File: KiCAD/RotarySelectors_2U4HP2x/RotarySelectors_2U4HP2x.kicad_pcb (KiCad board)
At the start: 2 copper layers, 20.3 x 84.1 mm, 8 parts, among them J1 Conn_01x08_Socket, J2 Conn_01x01_Socket, J3 Conn_01x08_Socket, J4 Conn_01x01_Socket

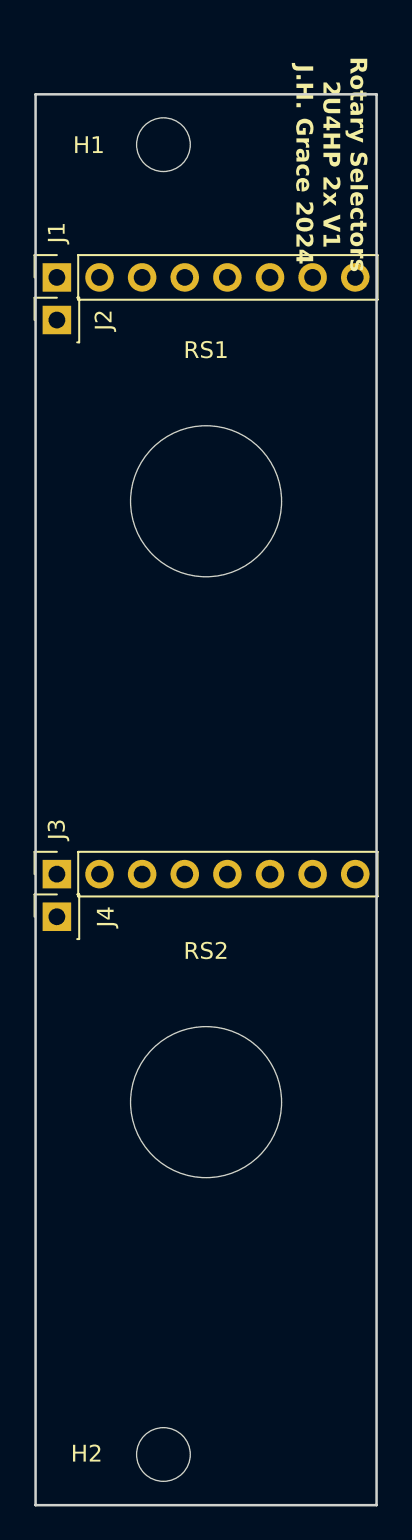
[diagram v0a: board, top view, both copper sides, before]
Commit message: updated PCB widths to better conform to Eurorack standards
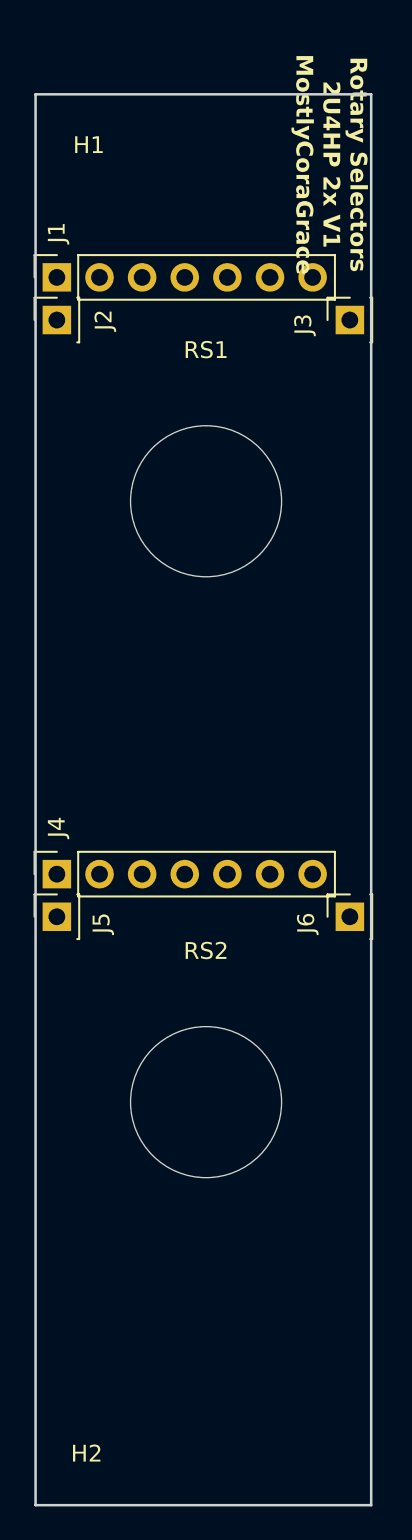
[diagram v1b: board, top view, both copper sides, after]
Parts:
- added J5: Conn_01x01_Socket, Connector_PinSocket_2.54mm:PinSocket_1x01_P2.54mm_Vertical, F.Cu at (1.27, 51.4)
- added J6: Conn_01x01_Socket, Connector_PinSocket_2.54mm:PinSocket_1x01_P2.54mm_Vertical, F.Cu at (18.7, 51.4)
- J1: value Conn_01x08_Socket -> Conn_01x07_Socket; footprint Connector_PinSocket_2.54mm:PinSocket_1x08_P2.54mm_Vertical -> Connector_PinSocket_2.54mm:PinSocket_1x07_P2.54mm_Vertical
- J3: value Conn_01x08_Socket -> Conn_01x01_Socket; footprint Connector_PinSocket_2.54mm:PinSocket_1x08_P2.54mm_Vertical -> Connector_PinSocket_2.54mm:PinSocket_1x01_P2.54mm_Vertical
- J4: value Conn_01x01_Socket -> Conn_01x07_Socket; footprint Connector_PinSocket_2.54mm:PinSocket_1x01_P2.54mm_Vertical -> Connector_PinSocket_2.54mm:PinSocket_1x07_P2.54mm_Vertical
- moved J3 37.4 mm to (18.7, 15.9)
- moved J4 2.54 mm to (1.27, 48.9)
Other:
- board size 20.3 x 84.1 mm -> 20 x 84.1 mm
- board text added: "Rotary Selectors 2U4HP 2x V1 MostlyCoraGrace"
- board text removed: "Rotary Selectors 2U4HP 2x V1 J.H. Grace 2024"

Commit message: removed all front silkscreen, and flipped most modules, to make the boards 'cleaner'.
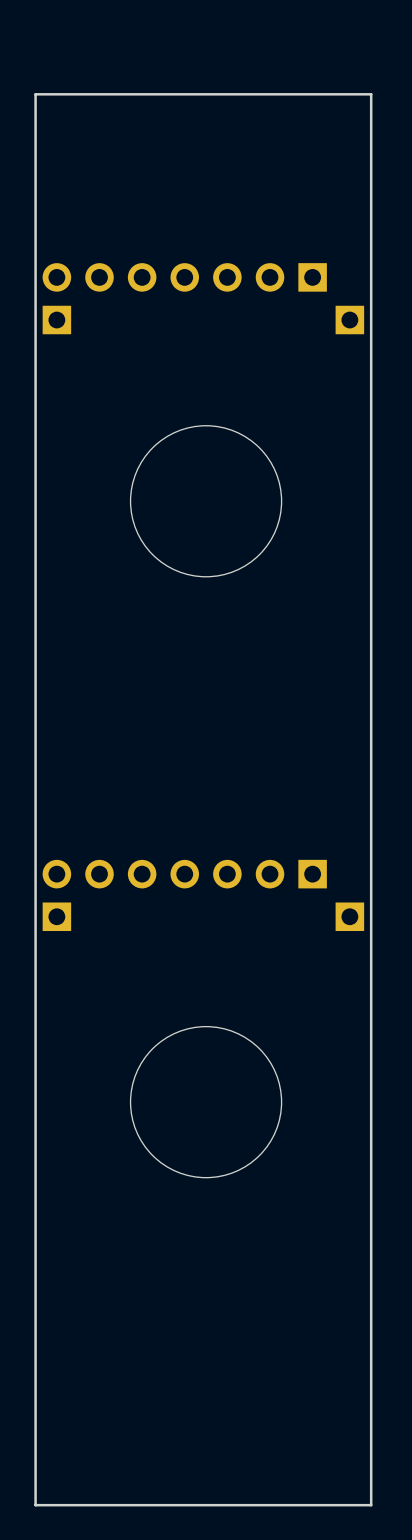
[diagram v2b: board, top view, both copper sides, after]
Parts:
- H1, H2, J1, J2, J3, J4, J5, J6, RS1, RS2: moved to B.Cu
- moved J1 15.2 mm to (16.5, 13.3)
- moved J4 15.2 mm to (16.5, 48.9)
- turned H1 to 180 degrees
- turned H2 to 180 degrees
- turned RS1 to 180 degrees
- turned RS2 to 180 degrees

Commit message: added copper fills to every module, to maybe possibly increase structural rigidity.
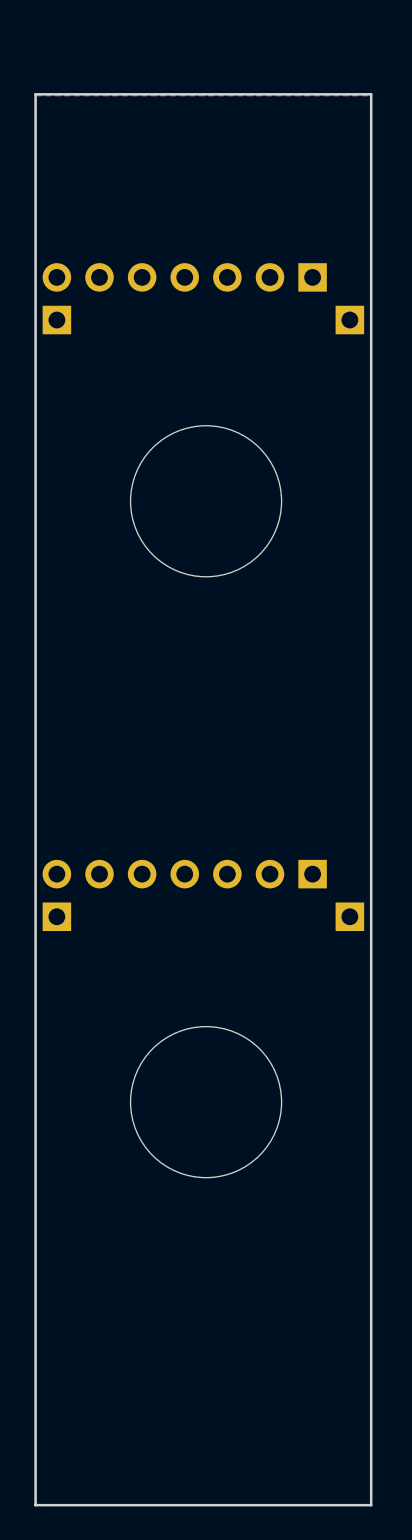
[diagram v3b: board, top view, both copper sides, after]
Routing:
- added copper zone on B.Cu, net (none)
- added copper zone on F.Cu, net (none)
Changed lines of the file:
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@@
 			)
 			(fill none)
-			(layer "Margin")
+			(layer "Dwgs.User")
 		)
 		(fp_circle
@@
 			)
 			(fill none)
-			(layer "F.CrtYd")
+			(layer "Dwgs.User")
 		)
 		(fp_text user "${REFERENCE}"
@@
 			)
 			(fill none)
-			(layer "Margin")
+			(layer "Dwgs.User")
 		)
 		(fp_circle
@@
 			)
 			(fill none)
-			(layer "F.CrtYd")
+			(layer "Dwgs.User")
 		)
 		(fp_text user "${REFERENCE}"
@@
 		)
 	)
+	(zone
+		(net 0)
+		(net_name "")
+		(layers "F&B.Cu")
+		(hatch edge 0.5)
+		(connect_pads
+			(clearance 0.5)
+		)
+		(min_thickness 0.25)
+		(filled_areas_thickness no)
+		(fill yes
+			(thermal_gap 0.5)
+			(thermal_bridge_width 0.5)
+			(island_removal_mode 1)
+			(island_area_min 10)
+		)
+		(polygon
+			(pts
+				(xy 0 2.5) (xy 20 2.5) (xy 20 86.5) (xy 0 86.5)
+			)
+		)
+	)
